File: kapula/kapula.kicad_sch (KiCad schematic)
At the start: 161 parts, among them J1 Conn_02x10_Odd_Even, J12 U.FL, J13 U.FL, J3 Conn_02x10_Odd_Even, J4 Conn_ARM_JTAG_SWD_10, J5 U.FL, J9 U.FL, Q1 AO3401A, Q1 BSS84, Q2 AO3401A, Q3 AO3400A, Q5 AO3400A, Q6 AO3400A, T1 BW21S7511A01TF, T2 BW21S7511A01TF, T3 BW21S7511A01TF, T4 BW21S7511A01TF, U1 XC6206P332MR, U2 TP4054, U3 DW01+G, U5 EFR32FG14P233F256GM48-B, U6 XA213-G4J, X1 DSB221SDN, Y1 32768 Hz

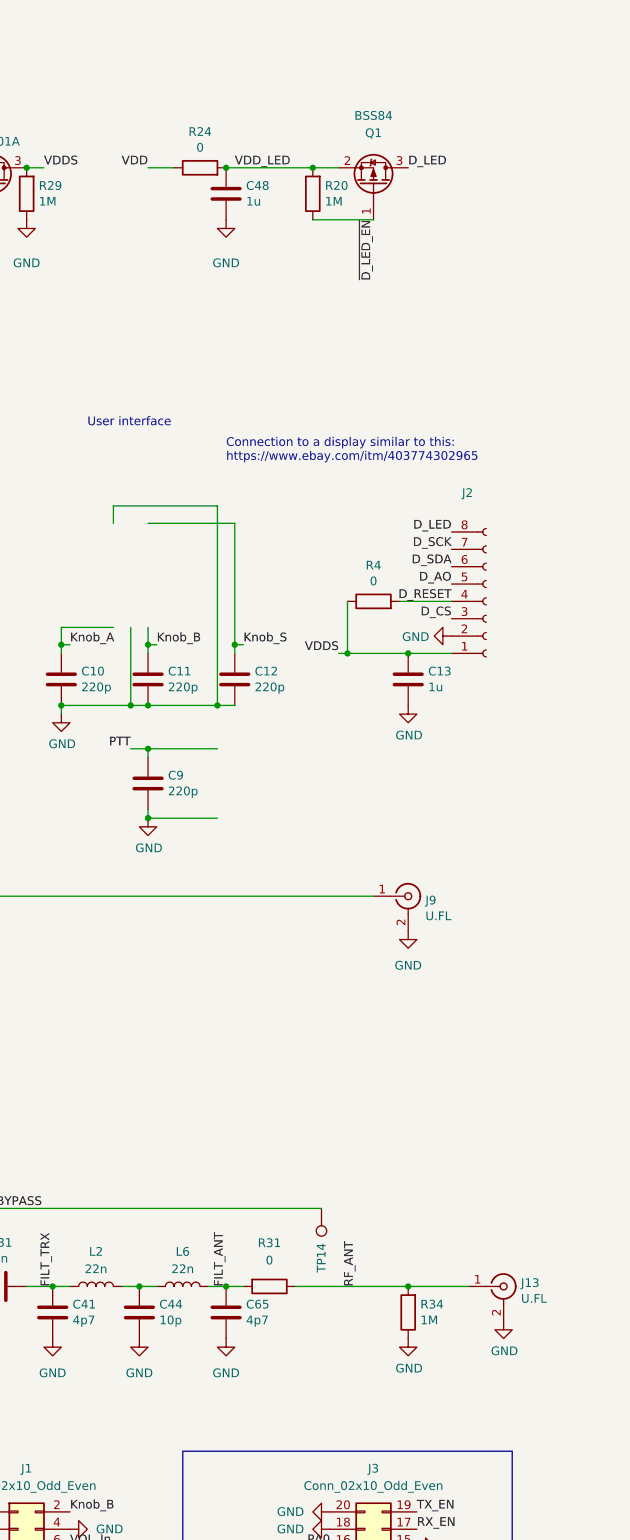
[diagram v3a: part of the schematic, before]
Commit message: PCB: Small circuit changes and layout improvements
* Add pads for extra series resistor for backlight
* Improve 2nd harmonic rejection of lowpass filter
* Move some components and vias a bit
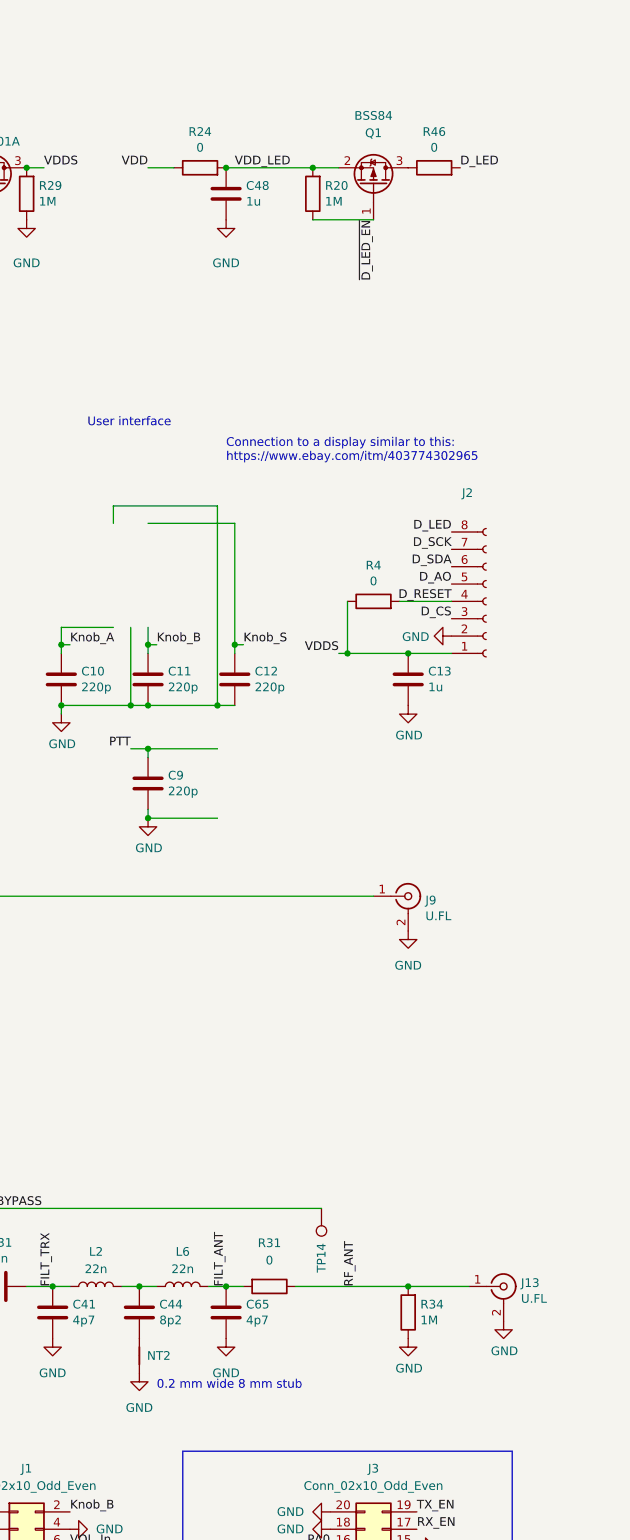
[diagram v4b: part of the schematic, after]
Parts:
- added NT2: ~, kapula:NetTie-2_SMD_Pad0.2mm, symbol kapula-rescue:Net-Tie_2-Device
- added R46: 0, Resistor_SMD:R_0402_1005Metric, symbol Device:R
- C44: value 10p -> 8p2; LCSC C32949 -> C1685
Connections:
- net D_LED: now also R46.2; no longer Q1.3 (D)
- net GND: now also NT2.2; no longer C44.2
- new net: C44.2, NT2.1
- new net: Q1.3 (D), R46.1
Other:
- note added: "0.2 mm wide 8 mm stub"
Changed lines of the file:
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@@
     (effects (font (size 1.27 1.27)) (justify left bottom))
   )
+  (text "0.2 mm wide 8 mm stub" (at 354.33 157.48 0)
+    (effects (font (size 1.27 1.27)) (justify left bottom))
+  )
   (text "Connection to a display similar to this:\nhttps://www.ebay.com/itm/403774302965"
     (at 364.49 21.59 0)
@@
     (effects (font (size 1.27 1.27)) (justify right bottom))
   )
-  (label "D_LED" (at 391.16 -21.59 0) (fields_autoplaced)
+  (label "D_LED" (at 398.78 -21.59 0) (fields_autoplaced)
     (effects (font (size 1.27 1.27)) (justify left bottom))
   )
@@
     )
   )
-  (symbol (lib_id "power:GND") (at 351.79 149.86 0) (unit 1)
+  (symbol (lib_id "power:GND") (at 351.79 154.94 0) (unit 1)
     (in_bom yes) (on_board yes) (dnp no) (fields_autoplaced)
-    (property "Reference" "#PWR0119" (at 351.79 156.21 0)
+    (property "Reference" "#PWR0119" (at 351.79 161.29 0)
       (effects (font (size 1.27 1.27)) hide)
     )
-    (property "Value" "GND" (at 351.79 154.94 0)
+    (property "Value" "GND" (at 351.79 160.02 0)
       (effects (font (size 1.27 1.27)))
     )
-    (property "Footprint" "" (at 351.79 149.86 0)
+    (property "Footprint" "" (at 351.79 154.94 0)
       (effects (font (size 1.27 1.27)) hide)
     )
-    (property "Datasheet" "" (at 351.79 149.86 0)
+    (property "Datasheet" "" (at 351.79 154.94 0)
       (effects (font (size 1.27 1.27)) hide)
     )
@@
     )
   )
+  (symbol (lib_id "kapula-rescue:Net-Tie_2-Device") (at 351.79 152.4 270) (unit 1)
+    (in_bom yes) (on_board yes) (dnp no)
+    (property "Reference" "NT2" (at 352.9076 152.4 90)
+      (effects (font (size 1.27 1.27)) (justify left))
+    )
+    (property "Value" "~" (at 352.9076 153.543 90)
+      (effects (font (size 1.27 1.27)) (justify left))
+    )
+    (property "Footprint" "kapula:NetTie-2_SMD_Pad0.2mm" (at 351.79 152.4 0)
+      (effects (font (size 1.27 1.27)) hide)
+    )
+    (property "Datasheet" "" (at 351.79 152.4 0)
+      (effects (font (size 1.27 1.27)) hide)
+    )
+    (pin "1")
+    (pin "2")
+    (instances
+      (project "kapula"
+        (path "/f2315993-072e-45c9-8c85-e79c6d40aba4"
+          (reference "NT2") (unit 1)
+        )
+      )
+    )
+  )
   (symbol (lib_id "Transistor_FET:AO3400A") (at 195.58 58.42 90) (mirror x) (unit 1)
     (in_bom yes) (on_board yes) (dnp no)
@@
       (effects (font (size 1.27 1.27)) (justify left))
     )
-    (property "Value" "10p" (at 354.711 147.193 0)
+    (property "Value" "8p2" (at 354.711 147.193 0)
       (effects (font (size 1.27 1.27)) (justify left))
     )
@@
       (effects (font (size 1.27 1.27)) hide)
     )
-    (property "LCSC" "C32949" (at 351.79 146.05 0)
+    (property "LCSC" "C1685" (at 351.79 146.05 0)
       (effects (font (size 1.27 1.27)) hide)
     )
@@
         )
       )
+    )
+  )
+  (symbol (lib_id "Device:R") (at 394.97 -21.59 90) (unit 1)
+    (in_bom yes) (on_board yes) (dnp no)
+    (property "Reference" "R46" (at 394.97 -26.8478 90)
+      (effects (font (size 1.27 1.27)))
+    )
+    (property "Value" "0" (at 394.97 -24.5364 90)
+      (effects (font (size 1.27 1.27)))
+    )
+    (property "Footprint" "Resistor_SMD:R_0402_1005Metric" (at 394.97 -19.812 90)
+      (effects (font (size 1.27 1.27)) hide)
+    )
+    (property "Datasheet" "" (at 394.97 -21.59 0)
+      (effects (font (size 1.27 1.27)) hide)
+    )
+    (property "LCSC" "C17168" (at 394.97 -21.59 0)
+      (effects (font (size 1.27 1.27)) hide)
+    )
+    (pin "1")
+    (pin "2")
+    (instances
+      (project "kapula"
+        (path "/f2315993-072e-45c9-8c85-e79c6d40aba4"
+          (reference "R46") (unit 1)
+        )
+      )

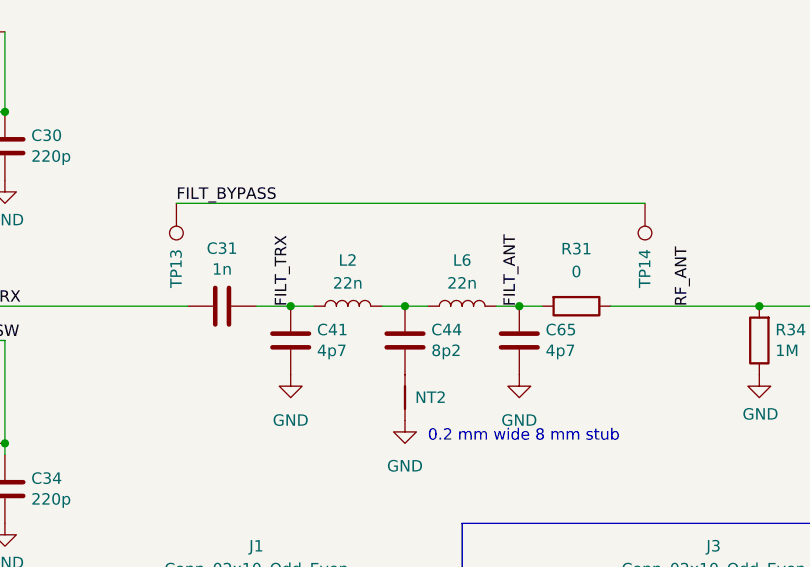
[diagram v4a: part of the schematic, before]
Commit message: PCB: Fix inductor value in lowpass filter
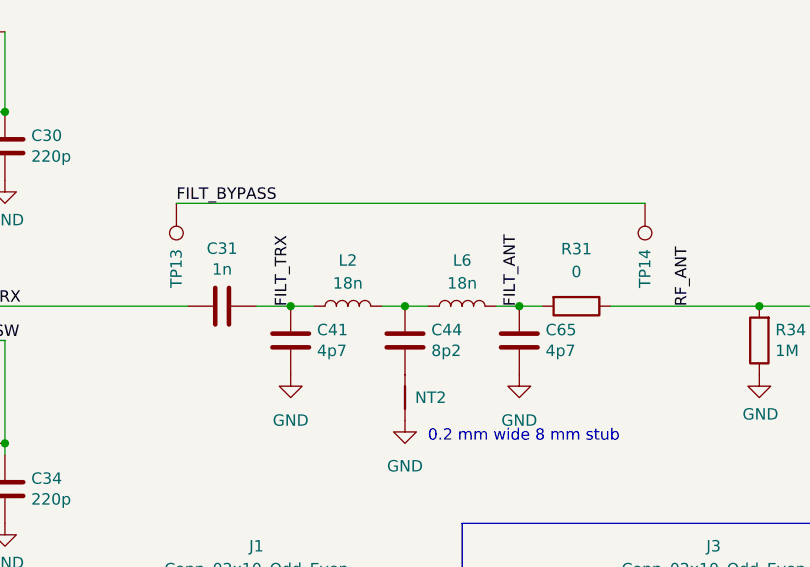
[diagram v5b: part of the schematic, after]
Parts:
- L2, L6: value 22n -> 18n; LCSC C12099 -> C48590
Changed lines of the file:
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@@
       (effects (font (size 1.27 1.27)) hide)
     )
-    (property "Datasheet" "" (at 195.58 127 0)
+    (property "Datasheet" "https://datasheet.lcsc.com/lcsc/2110081230_Sunlord-SDCL1005C47NJTDF_C27151.pdf" (at 195.58 127 0)
       (effects (font (size 1.27 1.27)) hide)
     )
@@
       (effects (font (size 1.27 1.27)) hide)
     )
-    (property "Datasheet" "" (at 195.58 137.16 0)
+    (property "Datasheet" "https://datasheet.lcsc.com/lcsc/2110081230_Sunlord-SDCL1005C47NJTDF_C27151.pdf" (at 195.58 137.16 0)
       (effects (font (size 1.27 1.27)) hide)
     )
@@
       (effects (font (size 1.27 1.27)))
     )
-    (property "Value" "22n" (at 358.14 139.7 90)
+    (property "Value" "18n" (at 358.14 139.7 90)
       (effects (font (size 1.27 1.27)))
     )
@@
       (effects (font (size 1.27 1.27)) hide)
     )
-    (property "Datasheet" "" (at 358.14 142.24 0)
+    (property "Datasheet" "https://datasheet.lcsc.com/lcsc/2110081230_Sunlord-SDCL1608C18NJTDF_C48590.pdf" (at 358.14 142.24 0)
       (effects (font (size 1.27 1.27)) hide)
     )
-    (property "LCSC" "C12099" (at 358.14 142.24 0)
+    (property "LCSC" "C48590" (at 358.14 142.24 0)
       (effects (font (size 1.27 1.27)) hide)
     )
@@
       (effects (font (size 1.27 1.27)))
     )
-    (property "Value" "22n" (at 345.44 139.7 90)
+    (property "Value" "18n" (at 345.44 139.7 90)
       (effects (font (size 1.27 1.27)))
     )
@@
       (effects (font (size 1.27 1.27)) hide)
     )
-    (property "Datasheet" "" (at 345.44 142.24 0)
+    (property "Datasheet" "https://datasheet.lcsc.com/lcsc/2110081230_Sunlord-SDCL1608C18NJTDF_C48590.pdf" (at 345.44 142.24 0)
       (effects (font (size 1.27 1.27)) hide)
     )
-    (property "LCSC" "C12099" (at 345.44 142.24 0)
+    (property "LCSC" "C48590" (at 345.44 142.24 0)
       (effects (font (size 1.27 1.27)) hide)
     )

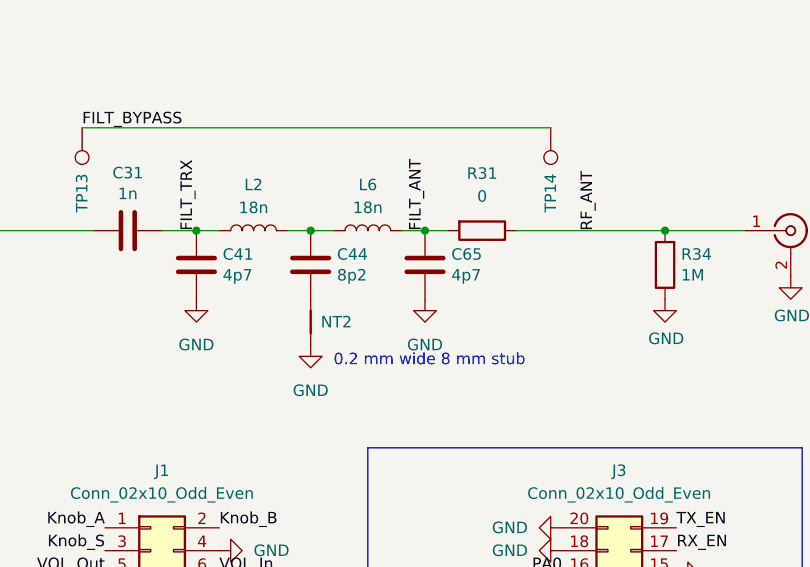
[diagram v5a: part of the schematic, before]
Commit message: PCB: Modify lowpass to use inductors from JLC basic series
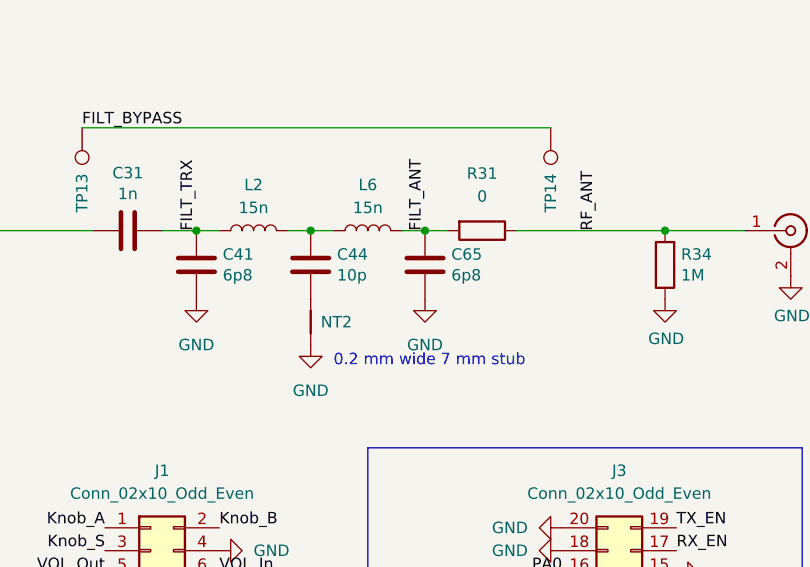
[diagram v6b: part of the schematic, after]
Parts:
- C41, C65: value 4p7 -> 6p8; LCSC C1569 -> C1679
- C44: value 8p2 -> 10p; LCSC C1685 -> C1634
- L2, L6: value 18n -> 15n; LCSC C48590 -> C27143
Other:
- note added: "0.2 mm wide 7 mm stub"
- note removed: "0.2 mm wide 8 mm stub"
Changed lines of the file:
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@@
     (effects (font (size 1.27 1.27)) (justify left bottom))
   )
-  (text "0.2 mm wide 8 mm stub" (at 354.33 157.48 0)
+  (text "0.2 mm wide 7 mm stub" (at 354.33 157.48 0)
     (effects (font (size 1.27 1.27)) (justify left bottom))
   )
@@
       (effects (font (size 1.27 1.27)) (justify left))
     )
-    (property "Value" "8p2" (at 354.711 147.193 0)
+    (property "Value" "10p" (at 354.711 147.193 0)
       (effects (font (size 1.27 1.27)) (justify left))
     )
@@
       (effects (font (size 1.27 1.27)) hide)
     )
-    (property "LCSC" "C1685" (at 351.79 146.05 0)
+    (property "LCSC" "C1634" (at 351.79 146.05 0)
       (effects (font (size 1.27 1.27)) hide)
     )
@@
       (effects (font (size 1.27 1.27)))
     )
-    (property "Value" "18n" (at 358.14 139.7 90)
+    (property "Value" "15n" (at 358.14 139.7 90)
       (effects (font (size 1.27 1.27)))
     )
@@
       (effects (font (size 1.27 1.27)) hide)
     )
-    (property "Datasheet" "https://datasheet.lcsc.com/lcsc/2110081230_Sunlord-SDCL1608C18NJTDF_C48590.pdf" (at 358.14 142.24 0)
+    (property "Datasheet" "https://datasheet.lcsc.com/lcsc/2110081230_Sunlord-SDCL1005C15NJTDF_C27143.pdf" (at 358.14 142.24 0)
       (effects (font (size 1.27 1.27)) hide)
     )
-    (property "LCSC" "C48590" (at 358.14 142.24 0)
+    (property "LCSC" "C27143" (at 358.14 142.24 0)
       (effects (font (size 1.27 1.27)) hide)
     )
@@
       (effects (font (size 1.27 1.27)) (justify left))
     )
-    (property "Value" "4p7" (at 367.411 147.193 0)
+    (property "Value" "6p8" (at 367.411 147.193 0)
       (effects (font (size 1.27 1.27)) (justify left))
     )
@@
       (effects (font (size 1.27 1.27)) hide)
     )
-    (property "LCSC" "C1569" (at 364.49 146.05 0)
+    (property "LCSC" "C1679" (at 364.49 146.05 0)
       (effects (font (size 1.27 1.27)) hide)
     )
@@
       (effects (font (size 1.27 1.27)))
     )
-    (property "Value" "18n" (at 345.44 139.7 90)
+    (property "Value" "15n" (at 345.44 139.7 90)
       (effects (font (size 1.27 1.27)))
     )
@@
       (effects (font (size 1.27 1.27)) hide)
     )
-    (property "Datasheet" "https://datasheet.lcsc.com/lcsc/2110081230_Sunlord-SDCL1608C18NJTDF_C48590.pdf" (at 345.44 142.24 0)
+    (property "Datasheet" "https://datasheet.lcsc.com/lcsc/2110081230_Sunlord-SDCL1005C15NJTDF_C27143.pdf" (at 345.44 142.24 0)
       (effects (font (size 1.27 1.27)) hide)
     )
-    (property "LCSC" "C48590" (at 345.44 142.24 0)
+    (property "LCSC" "C27143" (at 345.44 142.24 0)
       (effects (font (size 1.27 1.27)) hide)
     )
@@
       (effects (font (size 1.27 1.27)) (justify left))
     )
-    (property "Value" "4p7" (at 342.011 147.193 0)
+    (property "Value" "6p8" (at 342.011 147.193 0)
       (effects (font (size 1.27 1.27)) (justify left))
     )
@@
       (effects (font (size 1.27 1.27)) hide)
     )
-    (property "LCSC" "C1569" (at 339.09 146.05 0)
+    (property "LCSC" "C1679" (at 339.09 146.05 0)
       (effects (font (size 1.27 1.27)) hide)
     )

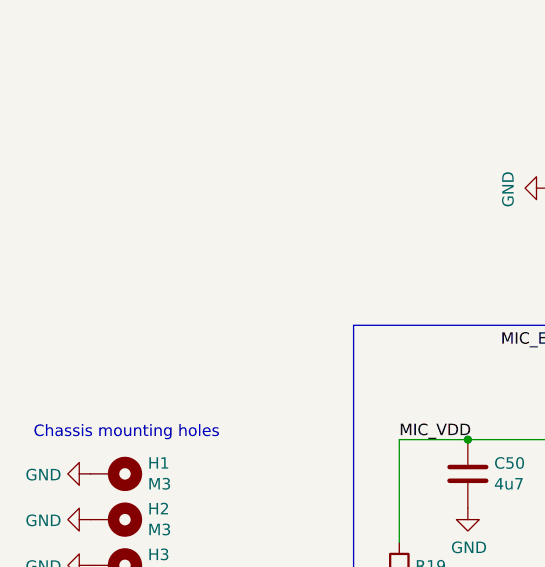
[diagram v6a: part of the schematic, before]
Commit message: PCB: Add tooling holes
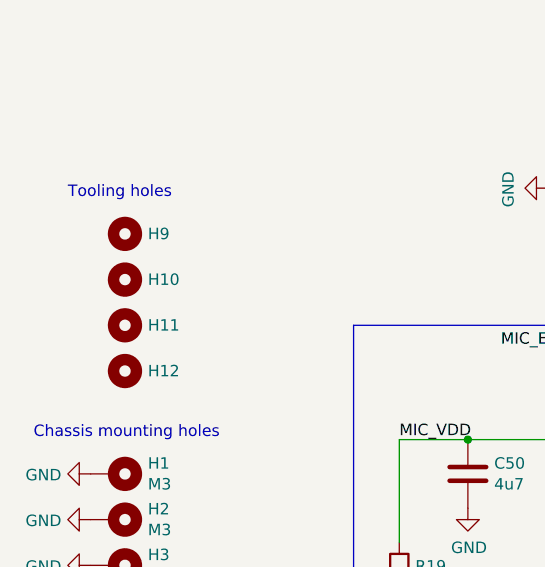
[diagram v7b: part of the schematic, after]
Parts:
- added H10, H11, H12, H9: ~, kapula:ToolingHole, symbol Mechanical:MountingHole
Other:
- note added: "Tooling holes"
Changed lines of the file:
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@@
     (effects (font (size 1.27 1.27)) (justify left bottom))
   )
+  (text "Tooling holes" (at 25.4 204.47 0)
+    (effects (font (size 1.27 1.27)) (justify left bottom))
+  )
   (text "AMP_SDN is pulled up to voltage higher than EFR32 supply\nbut it is connected to a 5 V tolerant pin so I think\nit should work by using the pin as an open drain output\nwith over-voltage tolerance enabled."
     (at 196.85 226.06 0)
@@
     )
   )
+  (symbol (lib_id "Mechanical:MountingHole") (at 31.75 223.52 0) (unit 1)
+    (in_bom yes) (on_board yes) (dnp no) (fields_autoplaced)
+    (property "Reference" "H12" (at 34.29 223.52 0)
+      (effects (font (size 1.27 1.27)) (justify left))
+    )
+    (property "Value" "~" (at 34.29 224.79 0)
+      (effects (font (size 1.27 1.27)) (justify left))
+    )
+    (property "Footprint" "kapula:ToolingHole" (at 31.75 223.52 0)
+      (effects (font (size 1.27 1.27)) hide)
+    )
+    (property "Datasheet" "" (at 31.75 223.52 0)
+      (effects (font (size 1.27 1.27)) hide)
+    )
+    (instances
+      (project "kapula"
+        (path "/f2315993-072e-45c9-8c85-e79c6d40aba4"
+          (reference "H12") (unit 1)
+        )
+      )
+    )
+  )
   (symbol (lib_id "Device:R") (at 215.9 261.62 90) (unit 1)
     (in_bom yes) (on_board yes) (dnp no) (fields_autoplaced)
@@
     )
   )
+  (symbol (lib_id "Mechanical:MountingHole") (at 31.75 213.36 0) (unit 1)
+    (in_bom yes) (on_board yes) (dnp no) (fields_autoplaced)
+    (property "Reference" "H10" (at 34.29 213.36 0)
+      (effects (font (size 1.27 1.27)) (justify left))
+    )
+    (property "Value" "~" (at 34.29 214.63 0)
+      (effects (font (size 1.27 1.27)) (justify left))
+    )
+    (property "Footprint" "kapula:ToolingHole" (at 31.75 213.36 0)
+      (effects (font (size 1.27 1.27)) hide)
+    )
+    (property "Datasheet" "" (at 31.75 213.36 0)
+      (effects (font (size 1.27 1.27)) hide)
+    )
+    (instances
+      (project "kapula"
+        (path "/f2315993-072e-45c9-8c85-e79c6d40aba4"
+          (reference "H10") (unit 1)
+        )
+      )
+    )
+  )
   (symbol (lib_id "Connector:TestPoint") (at 220.98 119.38 0) (unit 1)
     (in_bom yes) (on_board yes) (dnp no)
@@
     )
   )
+  (symbol (lib_id "Mechanical:MountingHole") (at 31.75 218.44 0) (unit 1)
+    (in_bom yes) (on_board yes) (dnp no) (fields_autoplaced)
+    (property "Reference" "H11" (at 34.29 218.44 0)
+      (effects (font (size 1.27 1.27)) (justify left))
+    )
+    (property "Value" "~" (at 34.29 219.71 0)
+      (effects (font (size 1.27 1.27)) (justify left))
+    )
+    (property "Footprint" "kapula:ToolingHole" (at 31.75 218.44 0)
+      (effects (font (size 1.27 1.27)) hide)
+    )
+    (property "Datasheet" "" (at 31.75 218.44 0)
+      (effects (font (size 1.27 1.27)) hide)
+    )
+    (instances
+      (project "kapula"
+        (path "/f2315993-072e-45c9-8c85-e79c6d40aba4"
+          (reference "H11") (unit 1)
+        )
+      )
+    )
+  )
   (symbol (lib_id "Device:R") (at 29.21 119.38 90) (unit 1)
     (in_bom yes) (on_board yes) (dnp no)
@@
         )
       )
+    )
+  )
+  (symbol (lib_id "Mechanical:MountingHole") (at 31.75 208.28 0) (unit 1)
+    (in_bom yes) (on_board yes) (dnp no) (fields_autoplaced)
+    (property "Reference" "H9" (at 34.29 208.28 0)
+      (effects (font (size 1.27 1.27)) (justify left))
+    )
+    (property "Value" "~" (at 34.29 209.55 0)
+      (effects (font (size 1.27 1.27)) (justify left))
+    )
+    (property "Footprint" "kapula:ToolingHole" (at 31.75 208.28 0)
+      (effects (font (size 1.27 1.27)) hide)
+    )
+    (property "Datasheet" "" (at 31.75 208.28 0)
+      (effects (font (size 1.27 1.27)) hide)
+    )
+    (instances
+      (project "kapula"
+        (path "/f2315993-072e-45c9-8c85-e79c6d40aba4"
+          (reference "H9") (unit 1)
+        )
+      )
